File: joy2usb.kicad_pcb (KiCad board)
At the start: 2 copper layers, 55 x 90 mm, 18 parts, among them J1 DB9_Male, J2 Conn_02x04_Odd_Even, SW1 RST, SW2 SW_SPDT, U1 Arduino_Pro_Micro, U2 4066

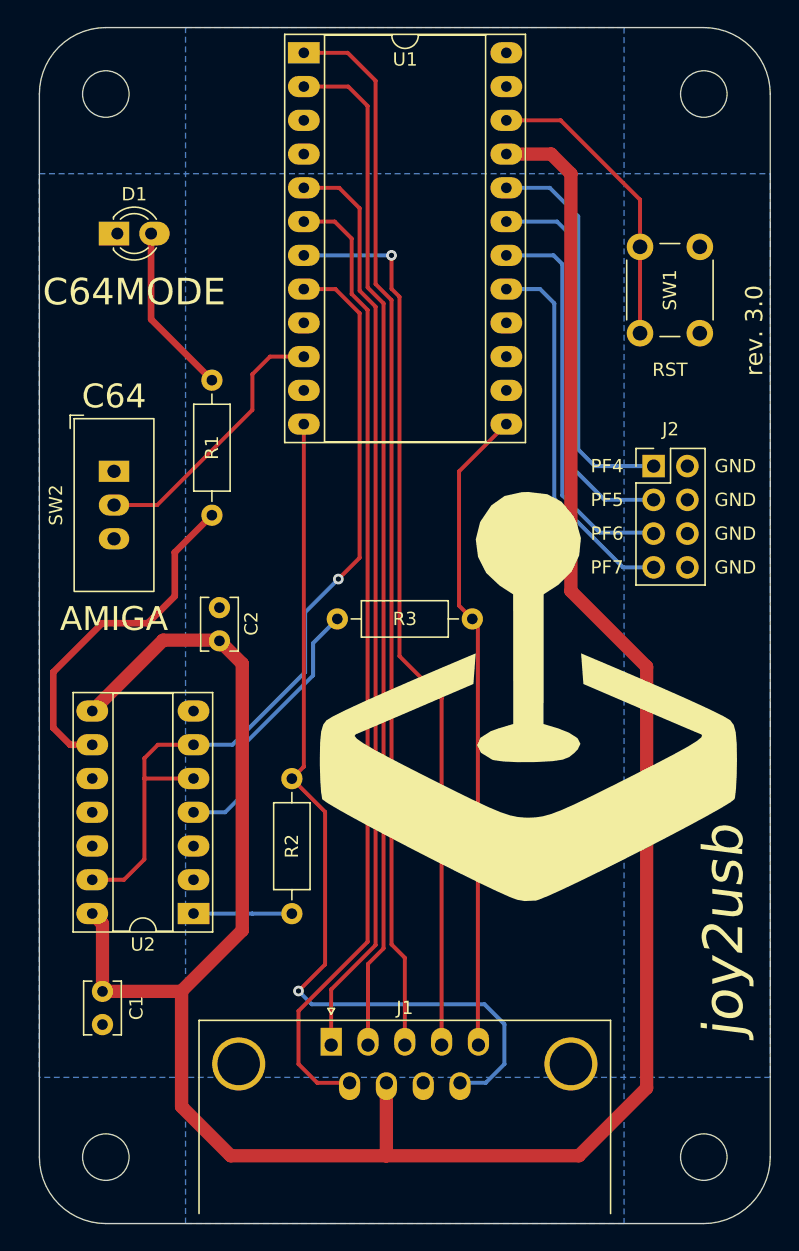
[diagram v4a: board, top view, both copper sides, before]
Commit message: PCB Rev. 3.1
Several cosmetic PCB updates
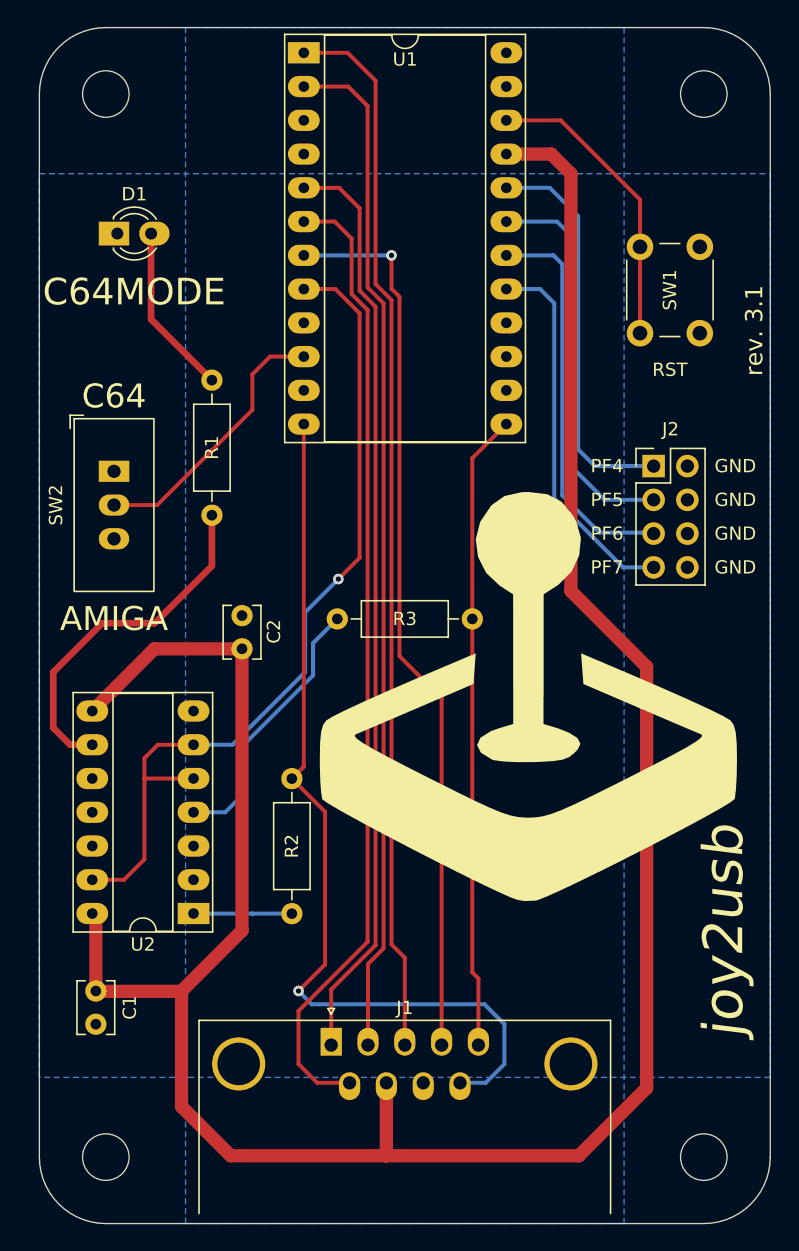
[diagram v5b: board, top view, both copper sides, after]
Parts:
- moved C2 1.80 mm to (128.2, 101.8)
- moved REF** 1.03 mm to (149.2, 113.5)
- moved C1 0.50 mm to (117.2, 127.5)
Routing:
- net /F3BTN: track 48.8 -> 48.0 mm
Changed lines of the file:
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@@
   (title_block
     (title "joy2usb")
-    (rev "3.0")
+    (rev "3.1")
     (company "mistepien")
   )
@@
   )
   (footprint "Capacitor_THT:C_Disc_D3.8mm_W2.6mm_P2.50mm" (layer "F.Cu")
-    (at 117.75 127.528 -90)
+    (at 117.25 127.5 -90)
     (descr "C, Disc series, Radial, pin pitch=2.50mm, , diameter*width=3.8*2.6mm^2, Capacitor, http://www.vishay.com/docs/45233/krseries.pdf")
     (tags "C Disc series Radial pin pitch 2.50mm  diameter 3.8mm width 2.6mm Capacitor")
@@
   )
   (footprint "Capacitor_THT:C_Disc_D3.8mm_W2.6mm_P2.50mm" (layer "F.Cu")
-    (at 126.55 101.15 90)
+    (at 128.25 101.75 90)
     (descr "C, Disc series, Radial, pin pitch=2.50mm, , diameter*width=3.8*2.6mm^2, Capacitor, http://www.vishay.com/docs/45233/krseries.pdf")
     (tags "C Disc series Radial pin pitch 2.50mm  diameter 3.8mm width 2.6mm Capacitor")
@@
   )
   (footprint "Symbol:OSHW-Logo_28.5x30mm_SilkScreen" (layer "B.Cu")
-    (at 149.5 112.5 90)
+    (at 149.25 113.5 90)
     (descr "Open Source Hardware Logo")
     (tags "Logo OSHW")
@@
   (via (at 139.5 72.14) (size 0.8) (drill 0.4) (layers "F.Cu" "B.Cu") (net 4))
   (segment (start 139.5 72.14) (end 132.9 72.14) (width 0.3) (layer "B.Cu") (net 4))
-  (segment (start 148.14 84.84) (end 144.58 88.4) (width 0.3) (layer "F.Cu") (net 5))
-  (segment (start 146 131.529669) (end 146.04 131.569669) (width 0.3) (layer "F.Cu") (net 5))
-  (segment (start 145.58 99.5) (end 146 99.92) (width 0.3) (layer "F.Cu") (net 5))
-  (segment (start 144.58 98.5) (end 145.58 99.5) (width 0.3) (layer "F.Cu") (net 5))
-  (segment (start 146 99.92) (end 146 131.529669) (width 0.3) (layer "F.Cu") (net 5))
-  (segment (start 144.58 88.4) (end 144.58 98.5) (width 0.3) (layer "F.Cu") (net 5))
+  (segment (start 148.14 84.84) (end 145.58 87.4) (width 0.3) (layer "F.Cu") (net 5))
+  (segment (start 145.58 99.5) (end 145.58 126.1) (width 0.3) (layer "F.Cu") (net 5))
+  (segment (start 145.58 126.1) (end 146.04 126.56) (width 0.3) (layer "F.Cu") (net 5))
+  (segment (start 146.04 126.56) (end 146.04 131.569669) (width 0.3) (layer "F.Cu") (net 5))
+  (segment (start 145.58 87.4) (end 145.58 99.5) (width 0.3) (layer "F.Cu") (net 5))
   (segment (start 137.7 76.251472) (end 137.7 123.8) (width 0.3) (layer "F.Cu") (net 6))
   (segment (start 132.9 69.6) (end 135.225 69.6) (width 0.3) (layer "F.Cu") (net 6))
@@
   (segment (start 158.7 134.8) (end 153.6 139.9) (width 1) (layer "F.Cu") (net 7))
   (segment (start 123.7 136.2) (end 127.4 139.9) (width 1) (layer "F.Cu") (net 7))
-  (segment (start 117.75 127.528) (end 117.75 122.441) (width 1) (layer "F.Cu") (net 7))
-  (segment (start 117.75 122.441) (end 116.98 121.671) (width 1) (layer "F.Cu") (net 7))
   (segment (start 158.7 103.1) (end 158.7 134.8) (width 1) (layer "F.Cu") (net 7))
-  (segment (start 122.311 101.1) (end 126.5 101.1) (width 1) (layer "F.Cu") (net 7))
-  (segment (start 126.5 101.1) (end 128.27 102.87) (width 1) (layer "F.Cu") (net 7))
+  (segment (start 117.25 121.941) (end 116.98 121.671) (width 1) (layer "F.Cu") (net 7))
+  (segment (start 117.25 127.5) (end 117.25 121.941) (width 1) (layer "F.Cu") (net 7))
+  (segment (start 117.278 127.528) (end 117.25 127.5) (width 1) (layer "F.Cu") (net 7))
+  (segment (start 123.678 127.528) (end 117.278 127.528) (width 1) (layer "F.Cu") (net 7))
   (segment (start 139.115 139.885) (end 139.1 139.9) (width 1) (layer "F.Cu") (net 7))
   (segment (start 148.14 64.52) (end 151.52 64.52) (width 1) (layer "F.Cu") (net 7))
-  (segment (start 116.98 106.431) (end 122.311 101.1) (width 1) (layer "F.Cu") (net 7))
+  (segment (start 128.25 122.956) (end 123.678 127.528) (width 1) (layer "F.Cu") (net 7))
   (segment (start 153 97.4) (end 158.7 103.1) (width 1) (layer "F.Cu") (net 7))
   (segment (start 139.115 134.409669) (end 139.115 139.885) (width 1) (layer "F.Cu") (net 7))
   (segment (start 123.7 136.2) (end 123.7 127.55) (width 1) (layer "F.Cu") (net 7))
-  (segment (start 128.27 122.936) (end 123.678 127.528) (width 1) (layer "F.Cu") (net 7))
+  (segment (start 121.661 101.75) (end 128.25 101.75) (width 1) (layer "F.Cu") (net 7))
   (segment (start 153 66) (end 153 97.4) (width 1) (layer "F.Cu") (net 7))
-  (segment (start 117.75 127.528) (end 123.678 127.528) (width 1) (layer "F.Cu") (net 7))
   (segment (start 153.6 139.9) (end 139.1 139.9) (width 1) (layer "F.Cu") (net 7))
+  (segment (start 128.25 101.75) (end 128.25 122.956) (width 1) (layer "F.Cu") (net 7))
+  (segment (start 116.98 106.431) (end 121.661 101.75) (width 1) (layer "F.Cu") (net 7))
   (segment (start 127.4 139.9) (end 139.1 139.9) (width 1) (layer "F.Cu") (net 7))
-  (segment (start 128.27 102.87) (end 128.27 122.936) (width 1) (layer "F.Cu") (net 7))
   (segment (start 123.7 127.55) (end 123.678 127.528) (width 1) (layer "F.Cu") (net 7))
   (segment (start 151.52 64.52) (end 153 66) (width 1) (layer "F.Cu") (net 7))
@@
   (segment (start 133 103.5) (end 127.534 108.966) (width 0.3) (layer "B.Cu") (net 24))
   (segment (start 133 99) (end 133 103.5) (width 0.3) (layer "B.Cu") (net 24))
+  (segment (start 116.98 108.971) (end 115.321 108.971) (width 0.5) (layer "F.Cu") (net 25))
+  (segment (start 114.046 107.696) (end 114.046 103.505) (width 0.5) (layer "F.Cu") (net 25))
+  (segment (start 121.678 99.822) (end 125.984 95.516) (width 0.5) (layer "F.Cu") (net 25))
+  (segment (start 125.984 95.516) (end 125.984 91.694) (width 0.5) (layer "F.Cu") (net 25))
+  (segment (start 115.321 108.971) (end 114.046 107.696) (width 0.5) (layer "F.Cu") (net 25))
+  (segment (start 117.729 99.822) (end 121.678 99.822) (width 0.5) (layer "F.Cu") (net 25))
   (segment (start 114.046 103.505) (end 117.729 99.822) (width 0.5) (layer "F.Cu") (net 25))
-  (segment (start 123.19 94.488) (end 126.05 91.628) (width 0.5) (layer "F.Cu") (net 25))
-  (segment (start 114.046 107.696) (end 114.046 103.505) (width 0.5) (layer "F.Cu") (net 25))
-  (segment (start 117.729 99.822) (end 121.158 99.822) (width 0.5) (layer "F.Cu") (net 25))
-  (segment (start 123.19 97.79) (end 123.19 94.488) (width 0.5) (layer "F.Cu") (net 25))
-  (segment (start 115.321 108.971) (end 114.046 107.696) (width 0.5) (layer "F.Cu") (net 25))
-  (segment (start 116.98 108.971) (end 115.321 108.971) (width 0.5) (layer "F.Cu") (net 25))
-  (segment (start 121.158 99.822) (end 123.19 97.79) (width 0.5) (layer "F.Cu") (net 25))
   (segment (start 129.018 121.68) (end 131.572 121.68) (width 0.3) (layer "B.Cu") (net 26))
   (segment (start 124.6 121.671) (end 129.009 121.671) (width 0.3) (layer "B.Cu") (net 26))

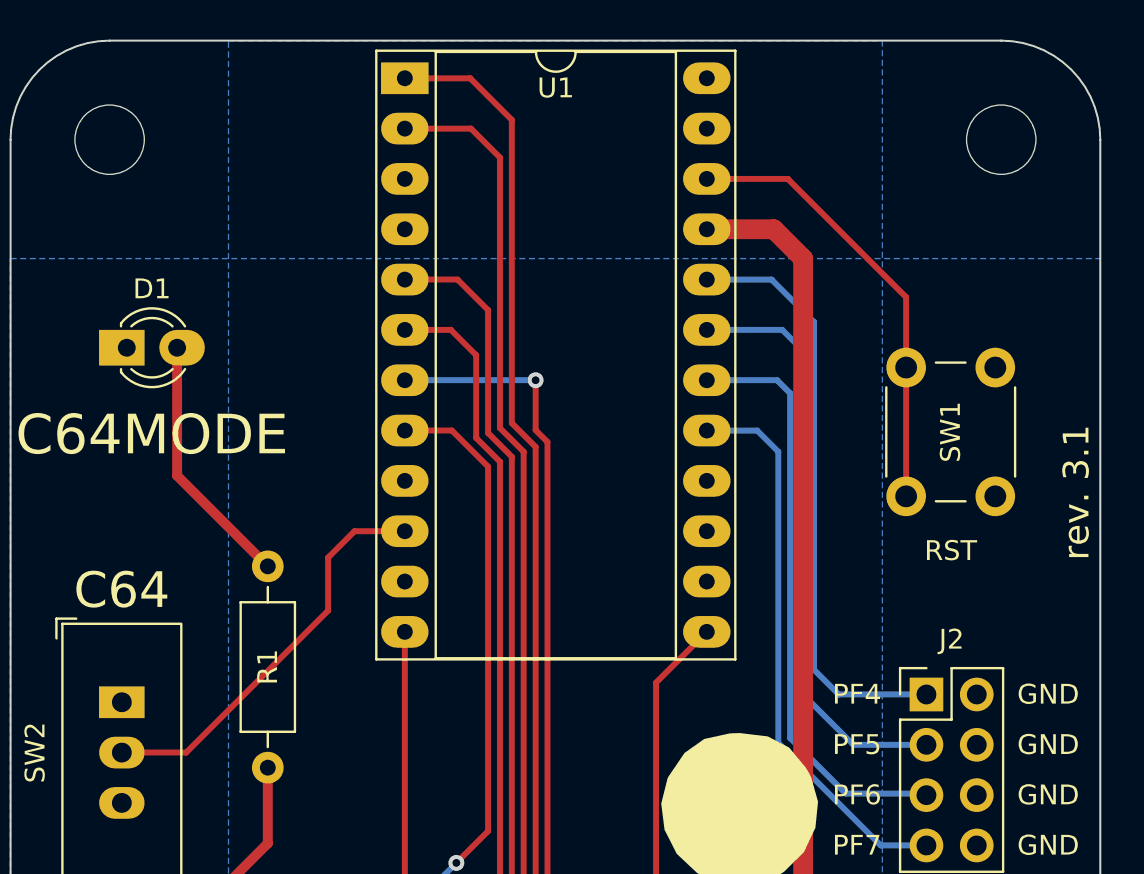
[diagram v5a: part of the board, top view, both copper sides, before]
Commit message: PCB Rev. 4.0
update C64/Amiga switch
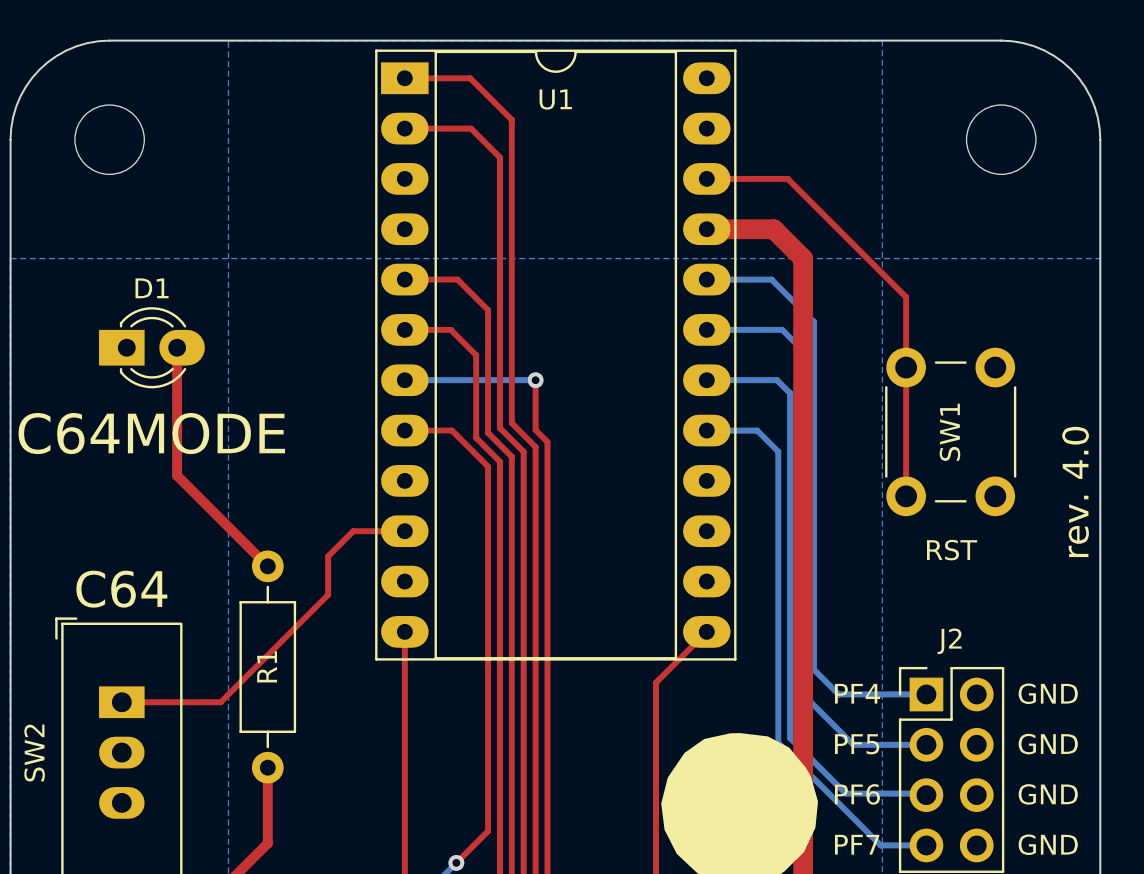
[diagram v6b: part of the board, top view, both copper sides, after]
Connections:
- SW2 pad 1: GND -> Net-(SW2-Pad1)
- SW2 pad 2: Net-(SW2-Pad2) -> GND
- SW2 pad 3: unconnected-(SW2-Pad3) -> GND
- U1 pad 10: Net-(SW2-Pad2) -> Net-(SW2-Pad1)
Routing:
- net Net-(SW2-Pad2): track 20.5 -> 0.00 mm
- net Net-(SW2-Pad1): track 0.00 -> 19.0 mm
